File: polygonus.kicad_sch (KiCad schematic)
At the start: 13 parts, among them J101 Conn_01x23, J102 Conn_01x35, J103 Conn_01x35, J105 Conn_01x01, J107 Conn_01x01, J108 Conn_01x01

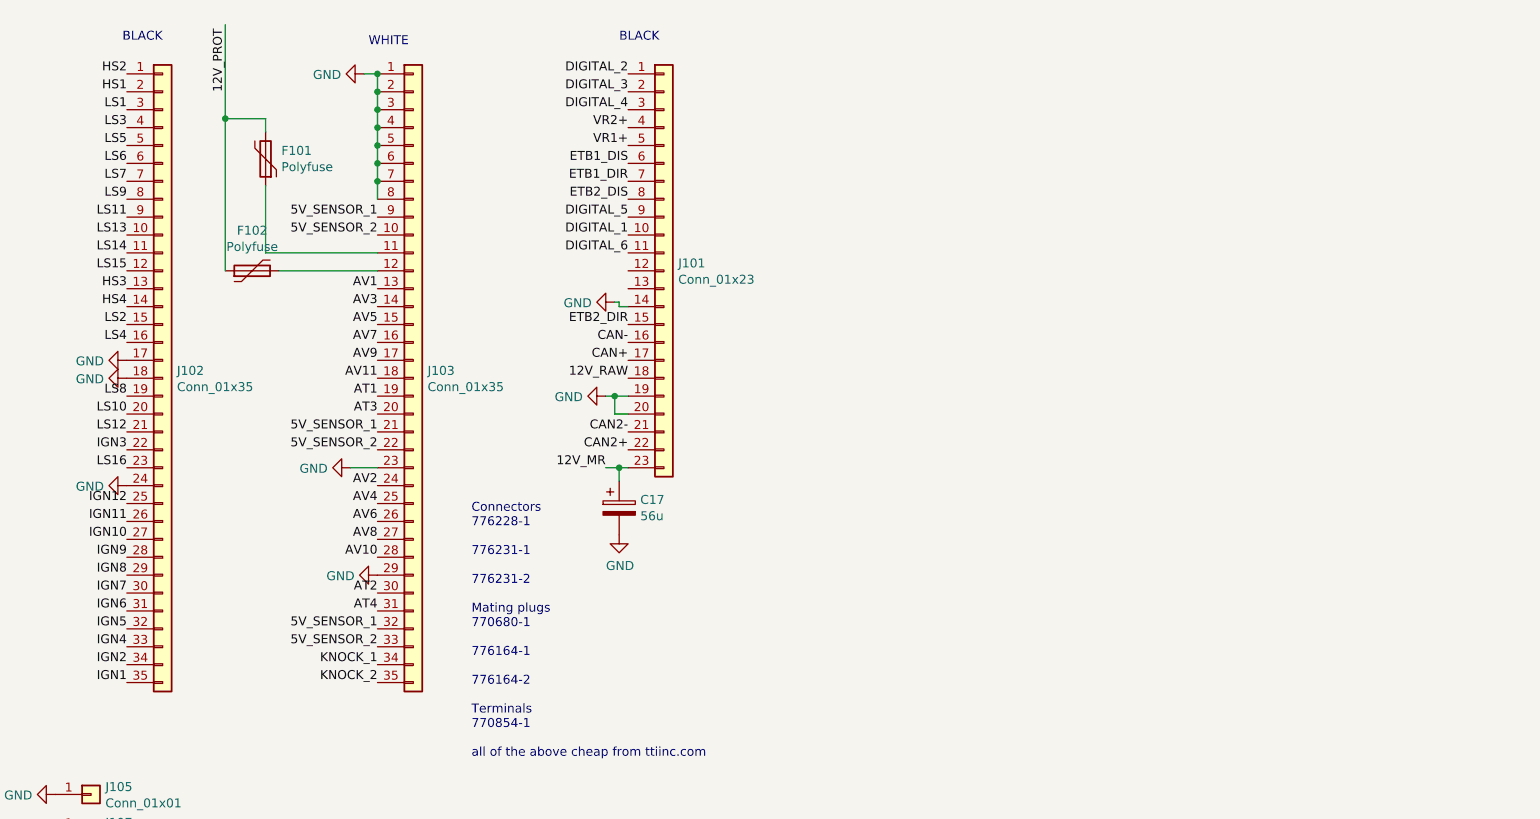
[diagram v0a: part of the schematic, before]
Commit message: Started moving to pin headers
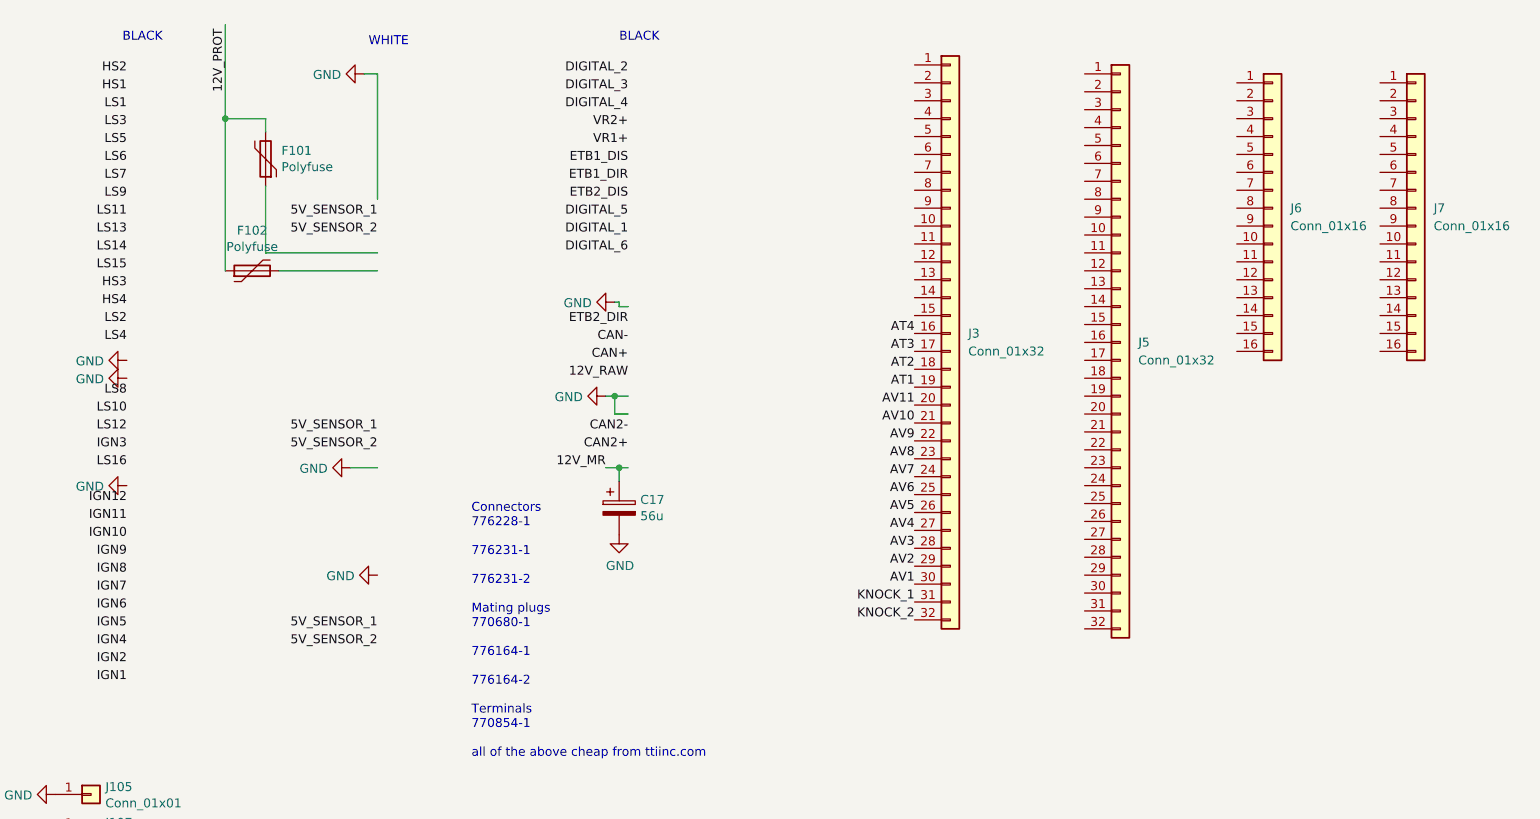
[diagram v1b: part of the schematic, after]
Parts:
- removed J101: Conn_01x23, ampseal:ampseal-23, symbol Connector_Generic:Conn_01x23
- removed J102: Conn_01x35, ampseal:ampseal-35, symbol Connector_Generic:Conn_01x35
- removed J103: Conn_01x35, ampseal:ampseal-35-2, symbol Connector_Generic:Conn_01x35
- added J3, J5: Conn_01x32, Connector_PinHeader_2.54mm:PinHeader_1x32_P2.54mm_Vertical, symbol Connector_Generic:Conn_01x32
- added J6, J7: Conn_01x16, Connector_PinHeader_2.54mm:PinHeader_1x16_P2.54mm_Vertical, symbol Connector_Generic:Conn_01x16
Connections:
- net AT1: now also J3.19 (Pin_19)
- net AT2: now also J3.18 (Pin_18)
- net AT3: now also J3.17 (Pin_17)
- net AT4: now also J3.16 (Pin_16)
- net AV1: now also J3.30 (Pin_30)
- net AV10: now also J3.21 (Pin_21)
- net AV11: now also J3.20 (Pin_20)
- net AV2: now also J3.29 (Pin_29)
- net AV3: now also J3.28 (Pin_28)
- net AV4: now also J3.27 (Pin_27)
- net AV5: now also J3.26 (Pin_26)
- net AV6: now also J3.25 (Pin_25)
- net AV7: now also J3.24 (Pin_24)
- net AV8: now also J3.23 (Pin_23)
- net AV9: now also J3.22 (Pin_22)
- net KNOCK_1: now also J3.31 (Pin_31)
- net KNOCK_2: now also J3.32 (Pin_32)

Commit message: Right hand pinout completed
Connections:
- net 5V_SENSOR_1: now also J3.7 (Pin_7), J3.8 (Pin_8), J3.9 (Pin_9)
- net 5V_SENSOR_2: now also J3.4 (Pin_4), J3.5 (Pin_5), J3.6 (Pin_6)
- net DIGITAL_1: now also J3.15 (Pin_15)
- net DIGITAL_2: now also J3.14 (Pin_14)
- net DIGITAL_3: now also J3.13 (Pin_13)
- net DIGITAL_4: now also J3.12 (Pin_12)
- net DIGITAL_5: now also J3.11 (Pin_11)
- net DIGITAL_6: now also J3.10 (Pin_10)
- net GND: now also J3.1 (Pin_1)
- net at F101.1: now also J3.2 (Pin_2)
- net at F102.2: now also J3.3 (Pin_3)
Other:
- moved on the sheet: J3

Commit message: Started left hand side
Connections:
- net LS13: now also J5.29 (Pin_29)
- net LS14: now also J5.30 (Pin_30)
- net LS15: now also J5.31 (Pin_31)
- net LS16: now also J5.32 (Pin_32)
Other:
- moved on the sheet: J5

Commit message: Stuff
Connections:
- net LS11: now also J5.27 (Pin_27)
- net LS12: now also J5.28 (Pin_28)
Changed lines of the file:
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@@
     (effects (font (size 1.27 1.27)) (justify right bottom))
   )
-  (label "LS11" (at 182.88 44.45 180)
+  (label "LS11" (at 195.58 90.17 180)
     (effects (font (size 1.27 1.27)) (justify right bottom))
   )
@@
     (effects (font (size 1.27 1.27)) (justify right bottom))
   )
-  (label "IGN12" (at 172.72 86.36 180)
+  (label "IGN12" (at 180.34 88.9 180)
     (effects (font (size 1.27 1.27)) (justify right bottom))
   )
@@
     (effects (font (size 1.27 1.27)) (justify left bottom))
   )
-  (label "LS12" (at 180.34 76.2 180)
+  (label "LS12" (at 195.58 92.71 180)
     (effects (font (size 1.27 1.27)) (justify right bottom))
   )

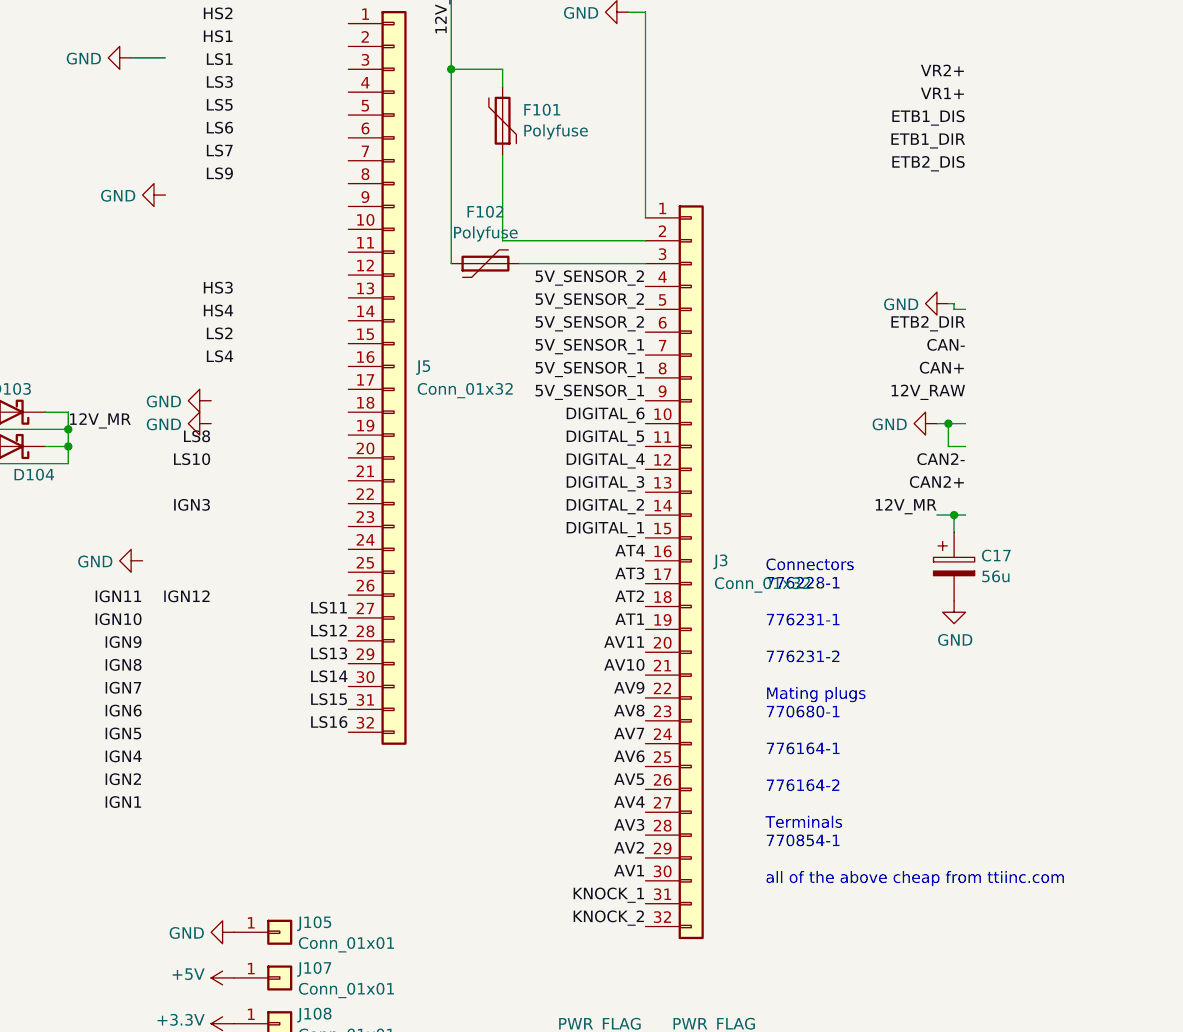
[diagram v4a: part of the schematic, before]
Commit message: Packaged LS13-16 with the flyback diodes
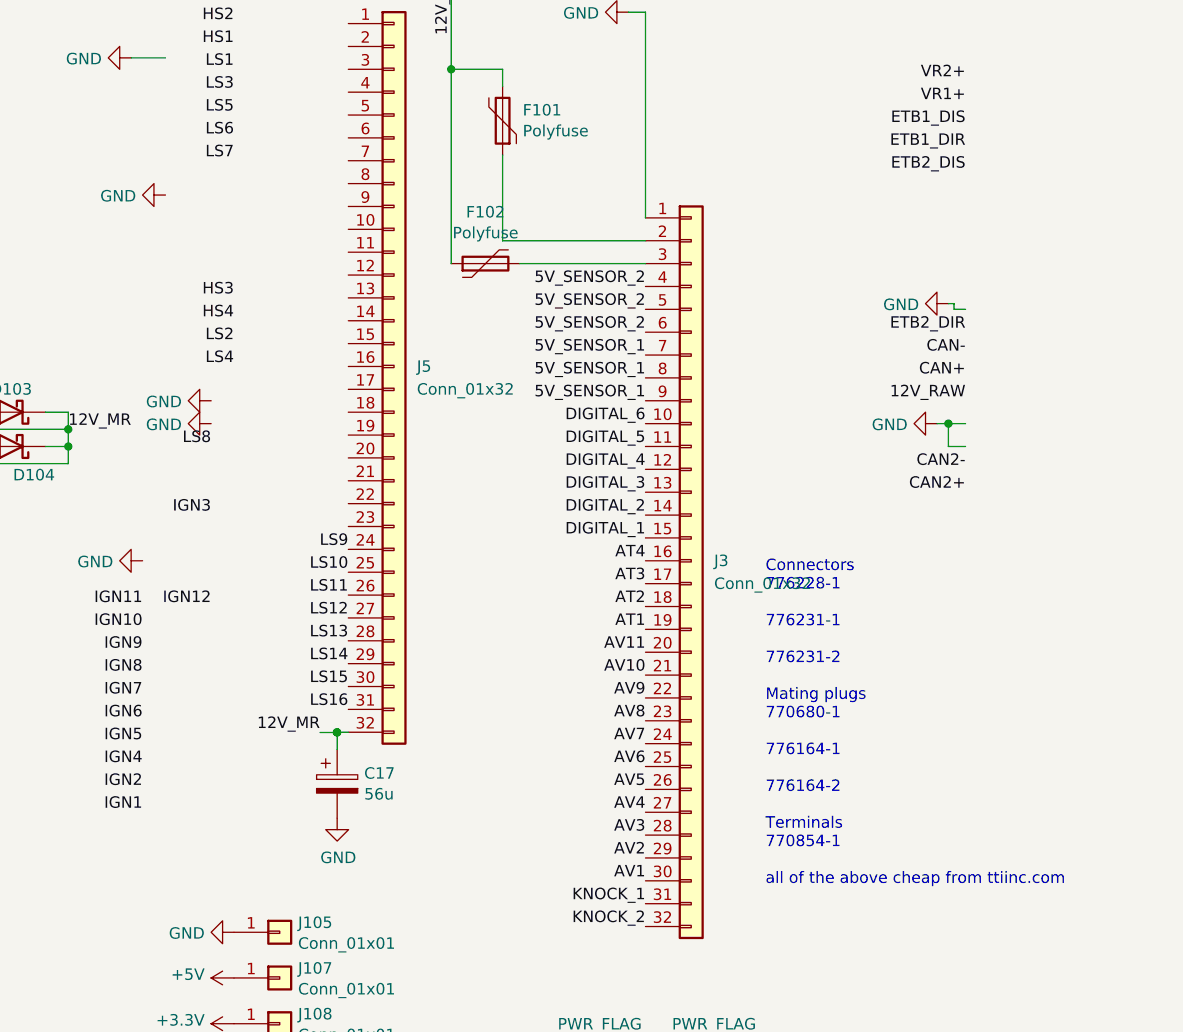
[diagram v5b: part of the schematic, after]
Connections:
- net 12V_MR: now also J5.32 (Pin_32)
- net LS10: now also J5.25 (Pin_25)
- net LS11: now also J5.26 (Pin_26); no longer J5.27 (Pin_27)
- net LS12: now also J5.27 (Pin_27); no longer J5.28 (Pin_28)
- net LS13: now also J5.28 (Pin_28); no longer J5.29 (Pin_29)
- net LS14: now also J5.29 (Pin_29); no longer J5.30 (Pin_30)
- net LS15: now also J5.30 (Pin_30); no longer J5.31 (Pin_31)
- net LS16: now also J5.31 (Pin_31); no longer J5.32 (Pin_32)
- net LS9: now also J5.24 (Pin_24)
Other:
- moved on the sheet: C17
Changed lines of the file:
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@@
   (junction (at 164.465 71.12) (diameter 0) (color 0 0 0 0)
   )
-  (junction (at 262.89 78.74) (diameter 0) (color 0 0 0 0)
+  (junction (at 194.343 102.899) (diameter 0) (color 0 0 0 0)
   )
   (junction (at 207.01 29.21) (diameter 0) (color 0 0 0 0)
@@
   (junction (at 262.255 68.58) (diameter 0) (color 0 0 0 0)
   )
+  (junction (at 194.31 102.87) (diameter 0) (color 0 0 0 0)
+  )
   (wire (pts (xy 62.23 144.145) (xy 68.58 144.145))
     (stroke (width 0) (type default) (color 0 0 0 0))
@@
     (stroke (width 0) (type default) (color 0 0 0 0))
   )
-  (wire (pts (xy 262.89 78.74) (xy 264.16 78.74))
+  (wire (pts (xy 194.31 102.87) (xy 195.58 102.87))
     (stroke (width 0) (type default) (color 0 0 0 0))
   )
@@
     (stroke (width 0) (type default) (color 0 0 0 0))
   )
-  (wire (pts (xy 260.985 78.74) (xy 262.89 78.74))
+  (wire (pts (xy 192.438 102.899) (xy 194.343 102.899))
     (stroke (width 0) (type default) (color 0 0 0 0))
   )
@@
     (stroke (width 0) (type default) (color 0 0 0 0))
   )
-  (wire (pts (xy 262.89 80.645) (xy 262.89 78.74))
+  (wire (pts (xy 194.343 104.804) (xy 194.343 102.899))
     (stroke (width 0) (type default) (color 0 0 0 0))
   )
@@
   )
   (wire (pts (xy 114.3 24.13) (xy 120.65 24.13))
+    (stroke (width 0) (type default) (color 0 0 0 0))
+  )
+  (wire (pts (xy 194.31 102.87) (xy 194.343 102.899))
     (stroke (width 0) (type default) (color 0 0 0 0))
   )
@@
     (effects (font (size 1.27 1.27)) (justify right bottom))
   )
-  (label "LS9" (at 182.88 41.91 180)
+  (label "LS9" (at 195.58 82.55 180)
     (effects (font (size 1.27 1.27)) (justify right bottom))
   )
@@
     (effects (font (size 1.27 1.27)) (justify right bottom))
   )
-  (label "LS16" (at 195.58 102.87 180)
+  (label "LS16" (at 195.58 100.33 180)
     (effects (font (size 1.27 1.27)) (justify right bottom))
   )
@@
     (effects (font (size 1.27 1.27)) (justify right bottom))
   )
-  (label "LS13" (at 195.58 95.25 180)
+  (label "LS13" (at 195.58 92.71 180)
     (effects (font (size 1.27 1.27)) (justify right bottom))
   )
@@
     (effects (font (size 1.27 1.27)) (justify right bottom))
   )
-  (label "12V_MR" (at 260.985 78.74 180)
+  (label "12V_MR" (at 192.438 102.899 180)
     (effects (font (size 1.27 1.27)) (justify right bottom))
   )
@@
     (effects (font (size 1.27 1.27)) (justify right bottom))
   )
-  (label "LS11" (at 195.58 90.17 180)
+  (label "LS11" (at 195.58 87.63 180)
     (effects (font (size 1.27 1.27)) (justify right bottom))
   )
@@
     (effects (font (size 1.27 1.27)) (justify left bottom))
   )
-  (label "LS15" (at 195.58 100.33 180)
+  (label "LS15" (at 195.58 97.79 180)
     (effects (font (size 1.27 1.27)) (justify right bottom))
   )
@@
     (effects (font (size 1.27 1.27)) (justify left bottom))
   )
-  (label "LS12" (at 195.58 92.71 180)
+  (label "LS12" (at 195.58 90.17 180)
     (effects (font (size 1.27 1.27)) (justify right bottom))
   )
@@
     (effects (font (size 1.27 1.27)) (justify left bottom))
   )
-  (label "LS10" (at 180.34 73.66 180)
+  (label "LS10" (at 195.58 85.09 180)
     (effects (font (size 1.27 1.27)) (justify right bottom))
   )
@@
     (effects (font (size 1.27 1.27)) (justify right bottom))
   )
-  (label "LS14" (at 195.58 97.79 180)
+  (label "LS14" (at 195.58 95.25 180)
     (effects (font (size 1.27 1.27)) (justify right bottom))
   )
@@
     (pin "2")
   )
-  (symbol (lib_id "Device:CP") (at 262.89 84.455 0) (unit 1)
-    (in_bom yes) (on_board yes)
-    (property "Reference" "C17" (id 0) (at 265.8872 83.2866 0)
+  (symbol (lib_id "Device:CP") (at 194.343 108.614 0) (unit 1)
+    (in_bom yes) (on_board yes)
+    (property "Reference" "C17" (id 0) (at 197.3402 107.4456 0)
       (effects (font (size 1.27 1.27)) (justify left))
     )
-    (property "Value" "56u" (id 1) (at 265.8872 85.598 0)
+    (property "Value" "56u" (id 1) (at 197.3402 109.757 0)
       (effects (font (size 1.27 1.27)) (justify left))
     )
-    (property "Footprint" "Capacitor_THT:CP_Radial_D8.0mm_P3.50mm" (id 2) (at 263.8552 88.265 0)
-      (effects (font (size 1.27 1.27)) hide)
-    )
-    (property "Datasheet" "~" (id 3) (at 262.89 84.455 0)
-      (effects (font (size 1.27 1.27)) hide)
-    )
-    (property "LCSC" "N/A" (id 4) (at 262.89 84.455 0)
-      (effects (font (size 1.27 1.27)) hide)
-    )
-    (property "PN" "EEH-AZF1H560B" (id 5) (at 262.89 84.455 0)
+    (property "Footprint" "Capacitor_THT:CP_Radial_D8.0mm_P3.50mm" (id 2) (at 195.3082 112.424 0)
+      (effects (font (size 1.27 1.27)) hide)
+    )
+    (property "Datasheet" "~" (id 3) (at 194.343 108.614 0)
+      (effects (font (size 1.27 1.27)) hide)
+    )
+    (property "LCSC" "N/A" (id 4) (at 194.343 108.614 0)
+      (effects (font (size 1.27 1.27)) hide)
+    )
+    (property "PN" "EEH-AZF1H560B" (id 5) (at 194.343 108.614 0)
       (effects (font (size 1.27 1.27)) hide)
     )
@@
     (pin "2")
   )
-  (symbol (lib_id "power:GND") (at 262.89 88.265 0) (unit 1)
-    (in_bom yes) (on_board yes)
-    (property "Reference" "#PWR0314" (id 0) (at 262.89 94.615 0)
-      (effects (font (size 1.27 1.27)) hide)
-    )
-    (property "Value" "GND" (id 1) (at 263.017 92.6592 0))
-    (property "Footprint" "" (id 2) (at 262.89 88.265 0)
-      (effects (font (size 1.27 1.27)) hide)
-    )
-    (property "Datasheet" "" (id 3) (at 262.89 88.265 0)
-      (effects (font (size 1.27 1.27)) hide)
-    )
+  (symbol (lib_id "power:GND") (at 194.343 112.424 0) (unit 1)
+    (in_bom yes) (on_board yes)
+    (property "Reference" "#PWR0314" (id 0) (at 194.343 118.774 0)
+      (effects (font (size 1.27 1.27)) hide)
+    )
+    (property "Value" "GND" (id 1) (at 194.47 116.8182 0))
+    (property "Footprint" "" (id 2) (at 194.343 112.424 0)
+      (effects (font (size 1.27 1.27)) hide)
+    )
+    (property "Datasheet" "" (id 3) (at 194.343 112.424 0)
+      (effects (font (size 1.27 1.27)) hide)
+    )

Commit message: Nearly finished routing
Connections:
- net +3V3: now also J6.2 (Pin_2)
- net 12V_MR: now also J5.3 (Pin_3)
- net 12V_RAW: now also J6.10 (Pin_10)
- net CAN+: now also J6.13 (Pin_13)
- net CAN-: now also J6.14 (Pin_14)
- net CAN2+: now also J7.9 (Pin_9)
- net CAN2-: now also J7.10 (Pin_10)
- net ETB1_DIR: now also J6.5 (Pin_5)
- net ETB1_DIS: now also J6.4 (Pin_4)
- net ETB1_PWM: now also J6.3 (Pin_3)
- net ETB2_DIR: now also J6.8 (Pin_8)
- net ETB2_DIS: now also J6.7 (Pin_7)
- net ETB2_PWM: now also J6.6 (Pin_6)
- net GND: now also J5.1 (Pin_1), J5.2 (Pin_2), J6.11 (Pin_11), J6.12 (Pin_12), J6.9 (Pin_9), J7.11 (Pin_11), J7.12 (Pin_12), J7.13 (Pin_13), J7.14 (Pin_14), J7.15 (Pin_15), J7.16 (Pin_16)
- net HS1: now also J7.4 (Pin_4)
- net HS2: now also J7.3 (Pin_3)
- net HS3: now also J7.2 (Pin_2)
- net HS4: now also J7.1 (Pin_1)
- net IGN1: now also J5.23 (Pin_23)
- net IGN10: now also J5.14 (Pin_14)
- net IGN11: now also J5.13 (Pin_13)
- net IGN12: now also J5.12 (Pin_12)
- net IGN2: now also J5.22 (Pin_22)
- net IGN3: now also J5.21 (Pin_21)
- net IGN4: now also J5.20 (Pin_20)
- net IGN5: now also J5.19 (Pin_19)
- net IGN6: now also J5.18 (Pin_18)
- net IGN7: now also J5.17 (Pin_17)
- net IGN8: now also J5.16 (Pin_16)
- net IGN9: now also J5.15 (Pin_15)
- net LS1: now also J5.4 (Pin_4)
- net LS2: now also J5.5 (Pin_5)
- net LS3: now also J5.6 (Pin_6)
- net LS4: now also J5.7 (Pin_7)
- net LS5: now also J5.8 (Pin_8)
- net LS6: now also J5.9 (Pin_9)
- net LS7: now also J5.10 (Pin_10)
- net LS8: now also J5.11 (Pin_11)
- net VR1+: now also J6.16 (Pin_16)
- net VR2+: now also J6.15 (Pin_15)
- net +5v: now reaches J6.1 (Pin_1)
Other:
- note added: "LEFT"
- note added: "RIGHT"
- note removed: "WHITE"
- moved on the sheet: F101, F102, J3, J6, J7

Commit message: Knocking down the errors
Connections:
- net +5v is gone; now on net +5V: J6.1 (Pin_1)
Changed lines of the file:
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@@
     (effects (font (size 1.27 1.27)) (justify right bottom))
   )
-  (label "+5v" (at 255.4645 49.8096 180)
+  (label "+5V" (at 255.4645 49.8096 180)
     (effects (font (size 1.27 1.27)) (justify right bottom))
   )
